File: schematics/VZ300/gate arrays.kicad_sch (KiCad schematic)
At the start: 5 parts, among them U10 GA3, U13 GA1, U14 GA2

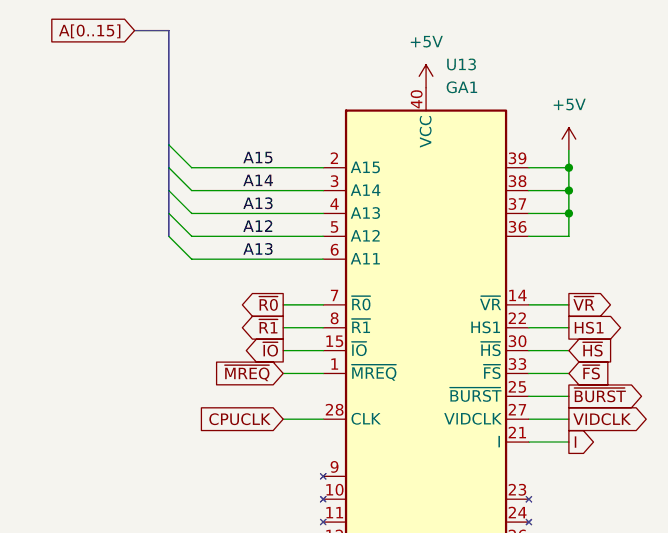
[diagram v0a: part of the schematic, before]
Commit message: Fix some minor issues in the VZ300 schematic
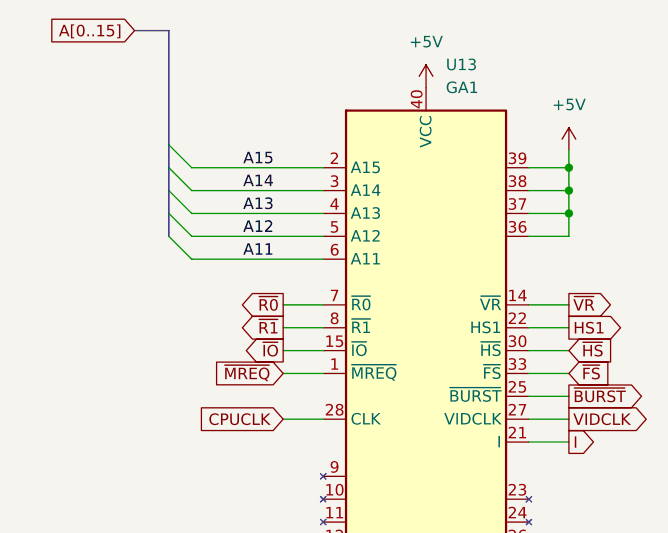
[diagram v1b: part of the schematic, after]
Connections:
- net A11: now also U13.6 (A11)
- net A13: no longer U13.6 (A11)
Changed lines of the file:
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@@
     (effects (font (size 1.27 1.27)) (justify left bottom))
   )
-  (label "A13" (at 50.165 72.39 0) (fields_autoplaced)
+  (label "A11" (at 50.165 72.39 0) (fields_autoplaced)
     (effects (font (size 1.27 1.27)) (justify left bottom))
   )
